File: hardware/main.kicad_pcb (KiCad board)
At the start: 2 copper layers, 100 x 72.4 mm, 18 parts, among them J4 Conn_01x01_Pin, J5 Conn_01x01_Pin, J6 Conn_01x01_Pin, K2 ADW11

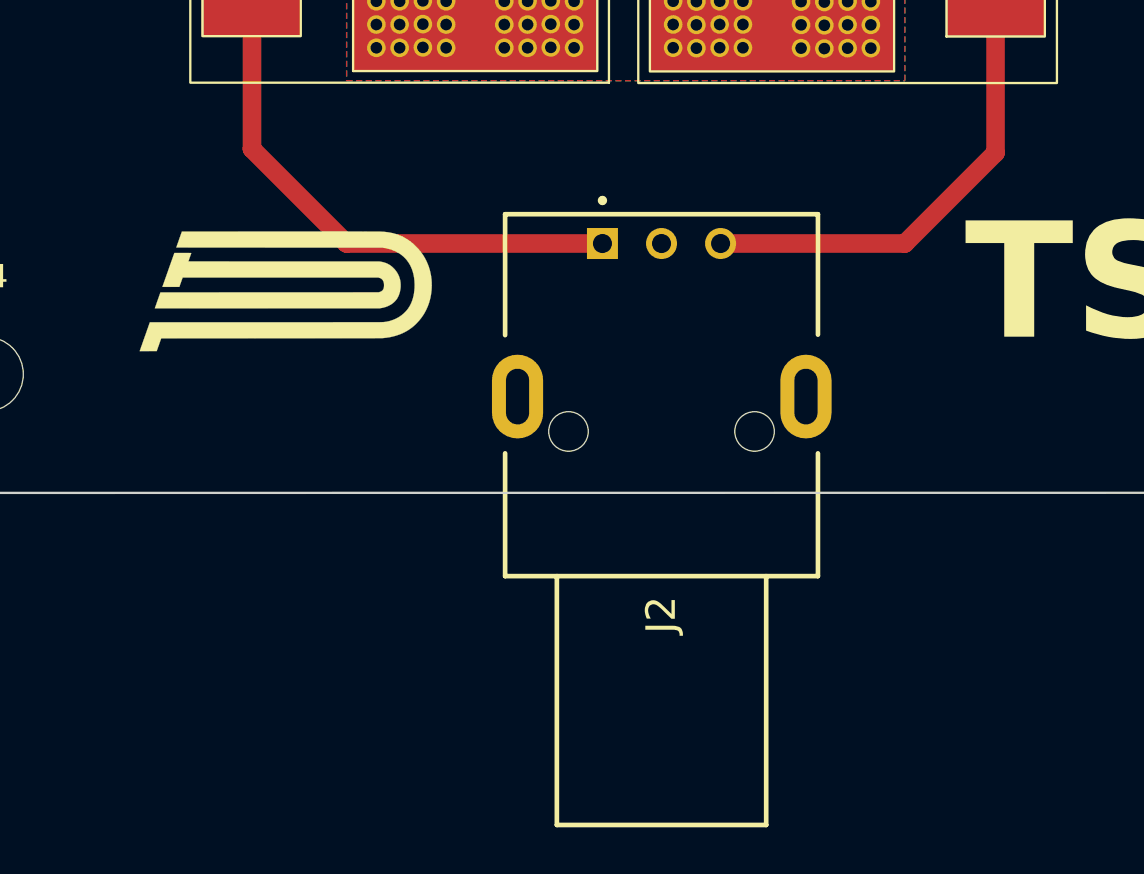
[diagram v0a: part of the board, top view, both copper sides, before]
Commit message: Changing the J2 connector
Adapting the connector to the existing harness for PM 09
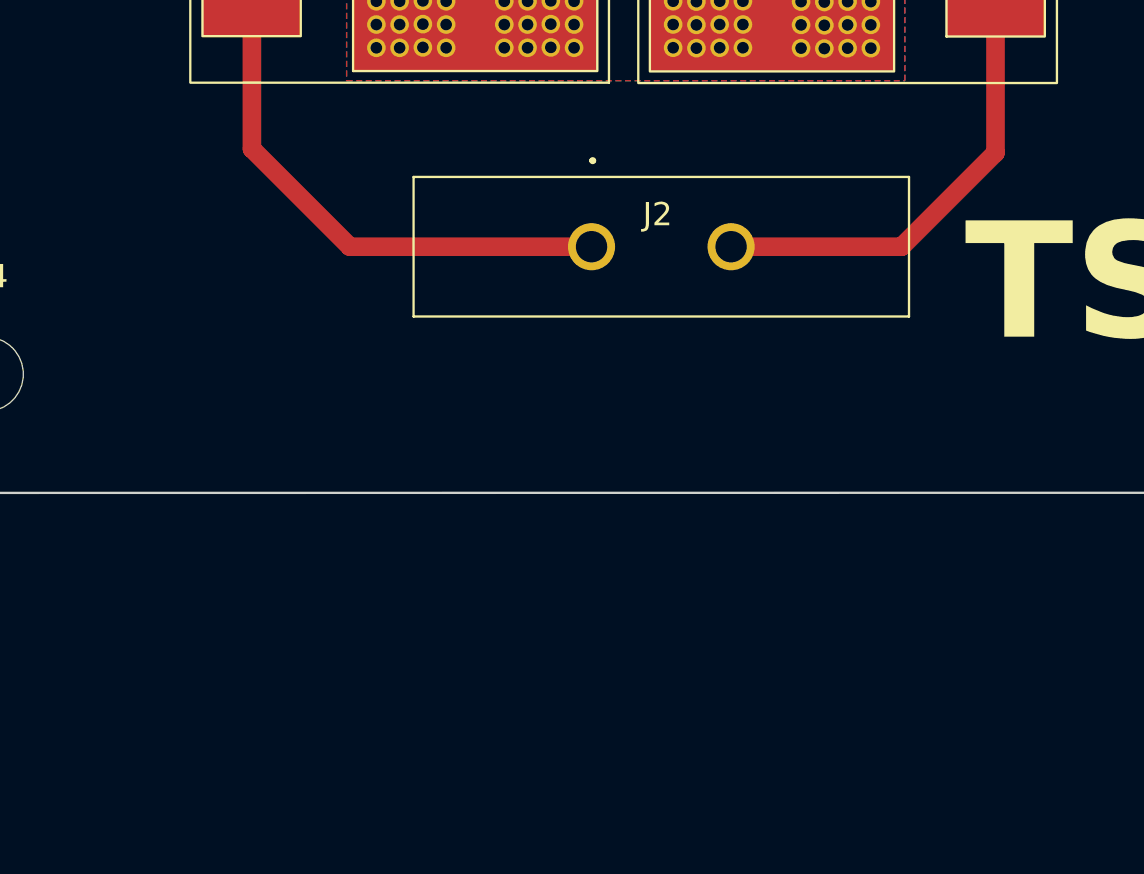
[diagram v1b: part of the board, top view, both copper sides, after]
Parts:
- removed G***: LOGO, put_silkscreen:PUTM_LOGO_15mm
- removed G***: LOGO, put_silkscreen:SignatureBox25mm
- J2: value ~ -> M300-MV10345M1; footprint d369-g33-xx:D369-G33-XX -> Samacsys:M300MV10345M1
- J4, J5, J6: value Conn_01x01_Pin -> ScrewTerminal
- R1: renamed from PWR263S-35-5001F1; value ~ -> PWR263S-35-5001F
- R2: renamed from PWR263S-35-5001F2; value ~ -> PWR263S-35-5001F
- R3: renamed from PWR263S-35-5001F3; value ~ -> PWR263S-35-5001F
- R4: renamed from PWR263S-35-5001F4; value ~ -> PWR263S-35-5001F
- R5: renamed from PWR263S-35-5001F5; value ~ -> PWR263S-35-5001F
- R6: renamed from PWR263S-35-5001F6; value ~ -> PWR263S-35-5001F
- moved J2 0.49 mm to (138.0, 107.8), turned to 180 degrees
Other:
- board text added: "J2"

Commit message: Zmniejszona
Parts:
- J1: value ~ -> Conn_01x04; footprint d369-g33-xx:D369-G33-XX -> Harwin_m80:HARWIN_M80-5100442
- moved H1 23.0 mm to (193.0, 72.0)
- moved H2 21.3 mm to (193.0, 94.0)
- moved H3 14.2 mm to (125.5, 55.0)
- moved H4 13.9 mm to (125.5, 110.0)
- moved J1 10.8 mm to (186.8, 82.2), turned to 90 degrees
- moved J6 9.55 mm to (134.7, 55.6), turned to -90 degrees
- moved R4 2.37 mm to (151.5, 97.1)
- moved R6 2.37 mm to (151.5, 70.9)
- moved J2 2.37 mm to (138.5, 110.1)
- moved R1 2.37 mm to (128.3, 70.9)
- moved R3 2.37 mm to (128.3, 97.1)
- moved R5 2.37 mm to (151.5, 84.0)
- moved R2 2.37 mm to (128.3, 84.0)
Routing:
- net HV+: track 9.82 -> 39.7 mm
- net GND: track 20.0 -> 8.37 mm
- net SD+: track 31.6 -> 20.2 mm
- net TSMP+: track 22.4 -> 18.9 mm
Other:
- board size 100 x 72.4 mm -> 76 x 65 mm

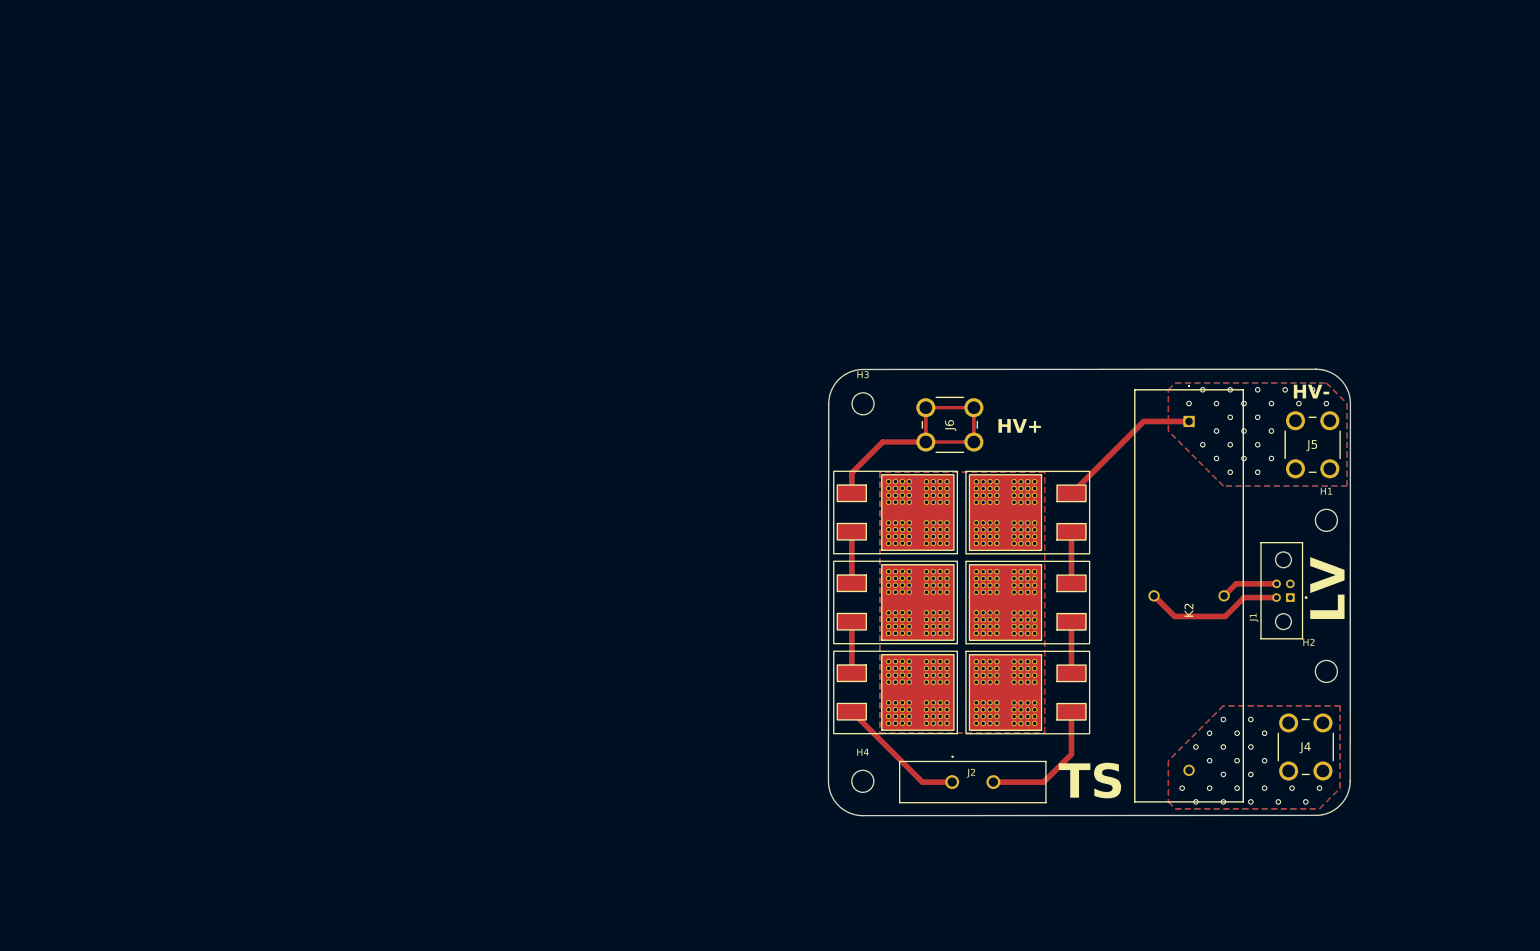
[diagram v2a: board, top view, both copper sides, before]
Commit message: Changed the creepage distance between HV and LV, changed thermal refielf for TSMP resistors
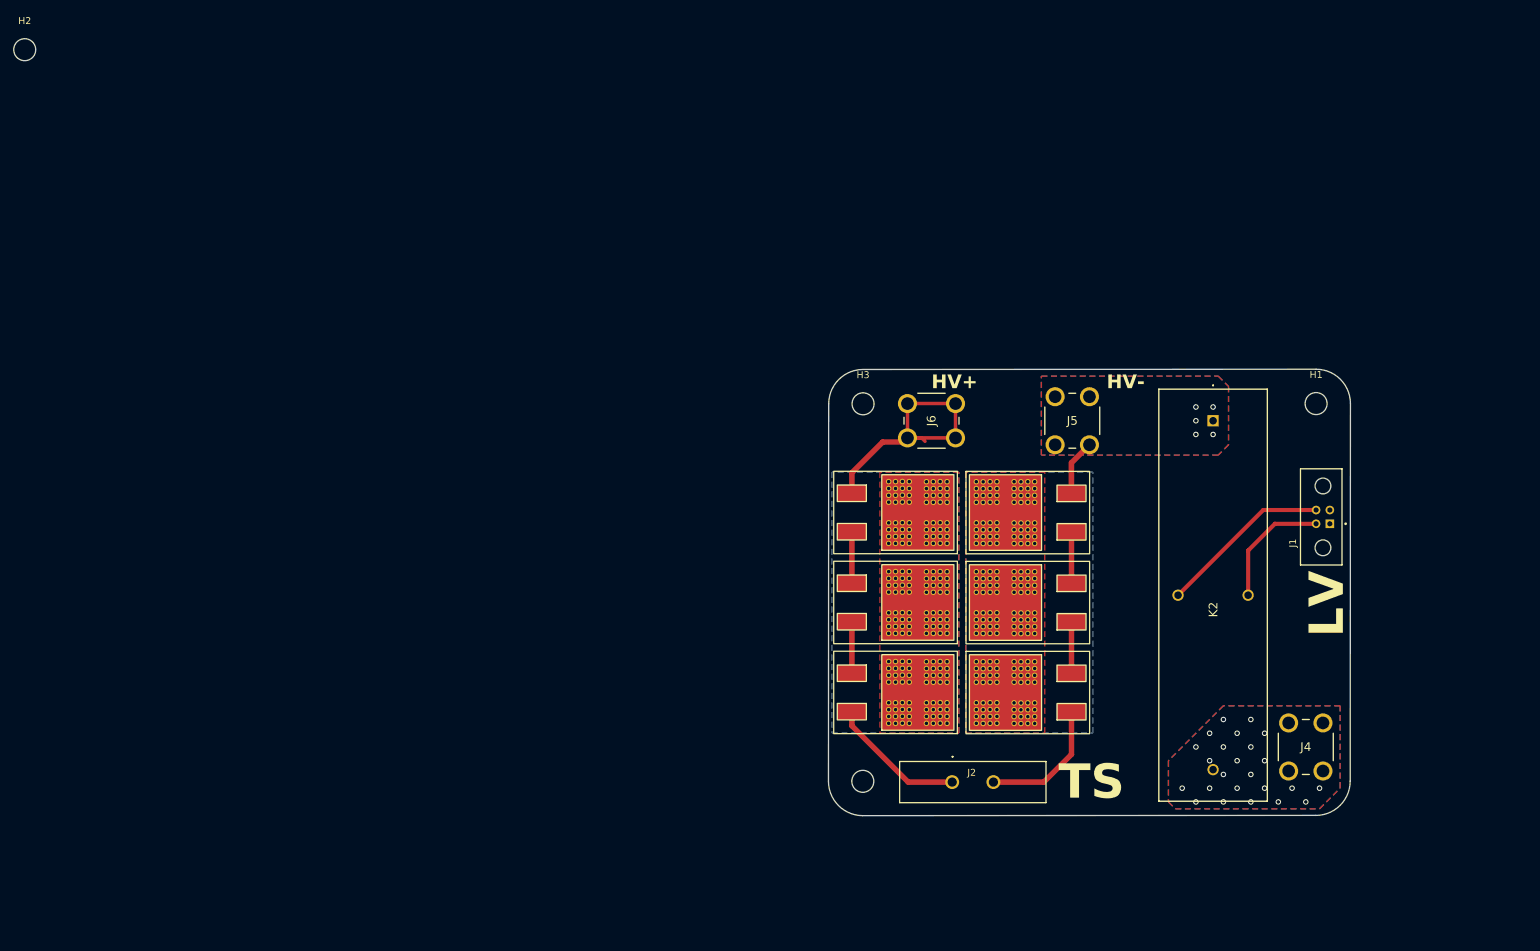
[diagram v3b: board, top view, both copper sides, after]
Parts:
- moved H2 210.0 mm to (3.48, 3.48)
- moved J5 35.2 mm to (153.5, 61.0)
- moved H1 17.1 mm to (191.5, 55.0)
- moved J1 12.2 mm to (192.5, 71.5)
- moved K2 3.50 mm to (176.5, 57.5)
- moved J6 2.74 mm to (132.0, 55.0)
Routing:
- net HV-: track 21.5 -> 8.35 mm, vias 24 -> 5
- net GND: track 8.37 -> 18.0 mm
- net SD+: track 20.2 -> 25.2 mm
- net TSMP+: track 18.9 -> 20.1 mm

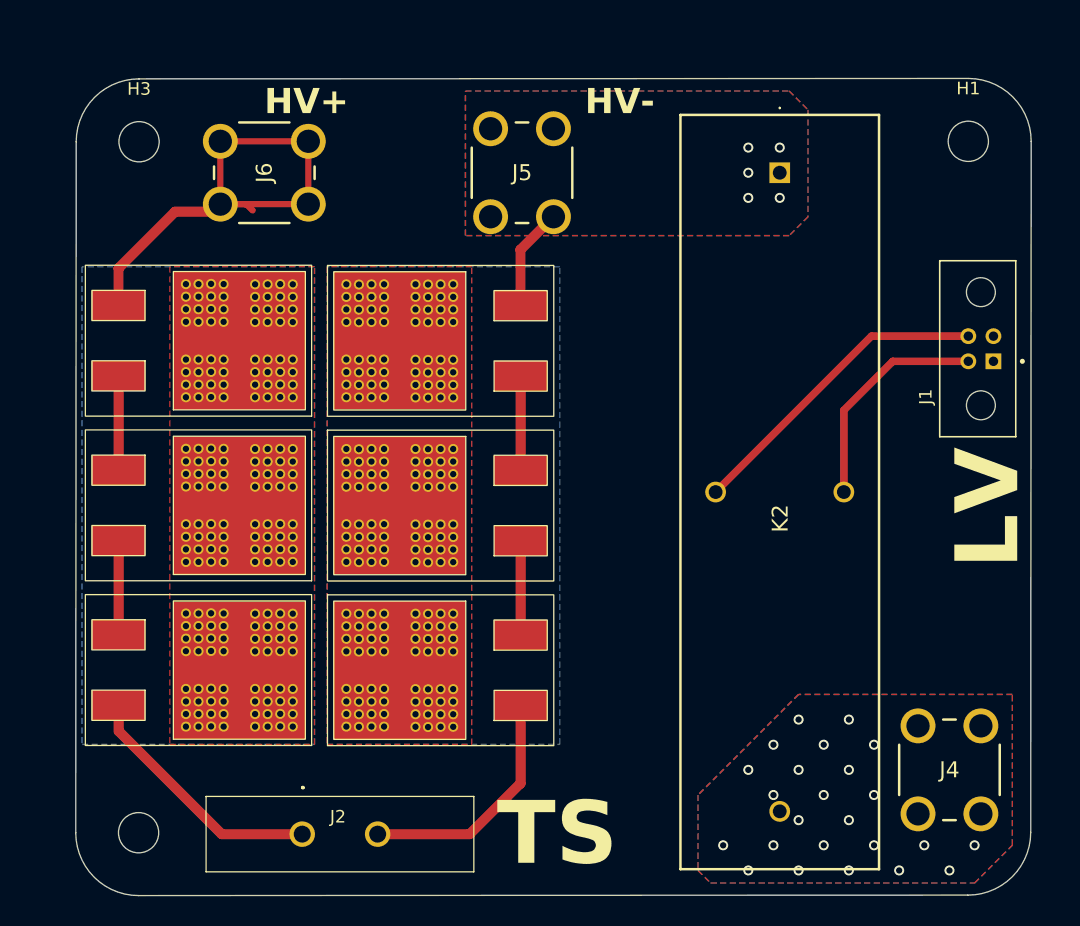
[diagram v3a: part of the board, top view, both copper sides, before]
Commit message: Usunięto rezystory discharge z pcb, zmniejszono płytkę
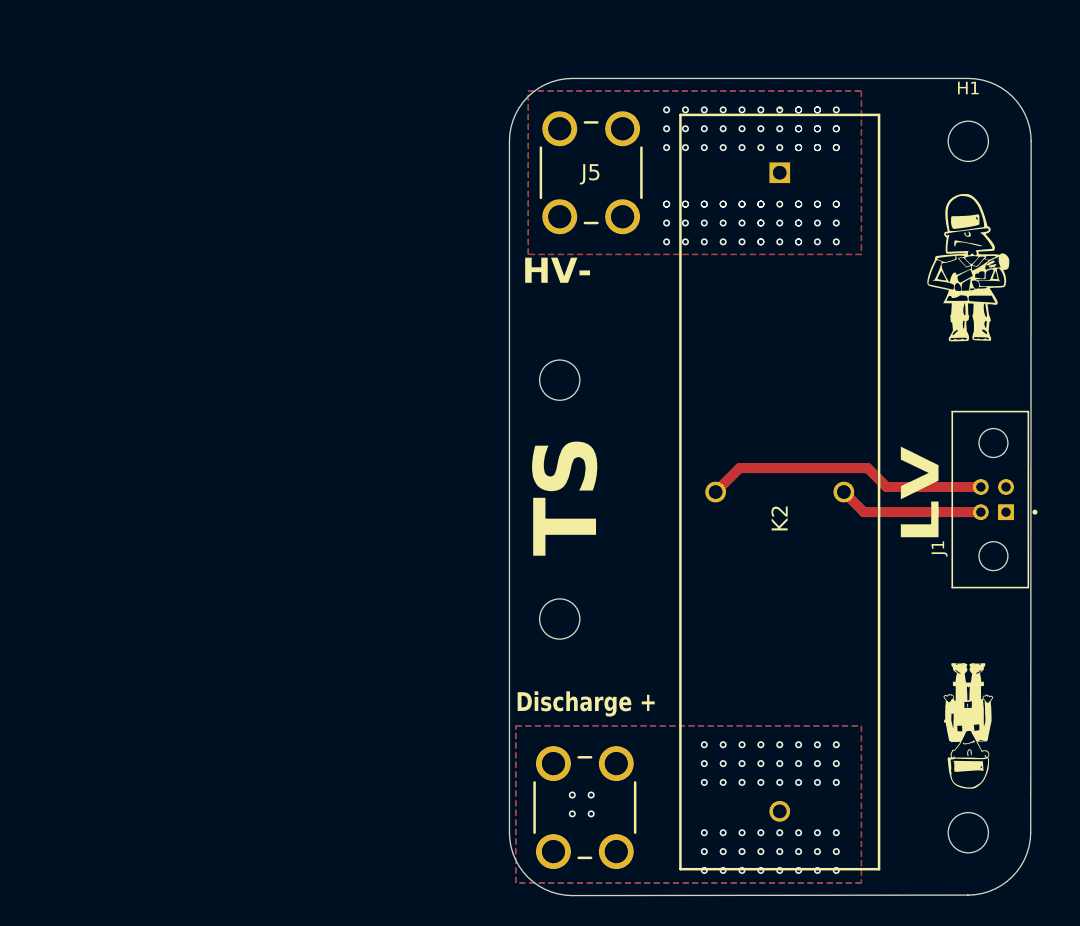
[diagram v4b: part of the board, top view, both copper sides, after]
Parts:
- removed J2: M300-MV10345M1, Samacsys:M300MV10345M1
- removed J6: ScrewTerminal, 7696:7696
- removed R1, R2, R3, R4, R5, R6: PWR263S-35-5001F, 7696:PWR263S-35-5001F
- added G***: LOGO, Cap:Sebek, F.Cu at (191.5, 101.5)
- added G***: LOGO, Cap:bomba_mniejszy, F.Cu at (191.5, 65.0)
- added H3: MountingHole, MountingHole:MountingHole_3.2mm_M3, F.Cu at (159.0, 93.0)
- moved H4 66.0 mm to (191.5, 110.0)
- moved H3 38.5 mm to (159.0, 74.0)
- moved J4 32.6 mm to (155.5, 114.5)
- moved J1 12.0 mm to (193.5, 83.5)
- moved J5 5.50 mm to (159.0, 61.0)
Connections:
- net Net-(J4-Pin_1) renamed /HV+_dIscharge_resistors
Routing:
- net HV+: track 39.9 -> 0.00 mm
- net TSMP+: track 20.1 -> 0.00 mm
- net TSMP-: track 19.2 -> 0.00 mm
- net HV-: track 8.35 -> 0.14 mm, vias 5 -> 87
- net Net-(R2-Pad2): track 7.50 -> 0.00 mm
- net Net-(R1-Pad2): track 7.50 -> 0.00 mm
- net Net-(R4-Pad2): track 7.50 -> 0.00 mm
- net Net-(R5-Pad2): track 7.50 -> 0.00 mm
- net GND: track 18.0 -> 11.6 mm
- net SD+: track 25.2 -> 22.5 mm
- net /HV+_dIscharge_resistors: vias 24 -> 52
- removed copper zone on B.Cu, net /THERMO
- removed copper zone on F.Cu, net /THERMO
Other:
- board size 76 x 65 mm -> 41.5 x 65 mm
- board text added: "Discharge +"
- board text removed: "HV+"
- board text removed: "J2"
